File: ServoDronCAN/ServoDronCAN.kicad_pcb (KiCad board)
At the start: 2 copper layers, 80 x 87 mm, 13 parts, among them J2 Conn_01x02_Pin, J3 Conn_01x02_Pin, Q1 IRF9530N, U2 LM2575BU-ADJ

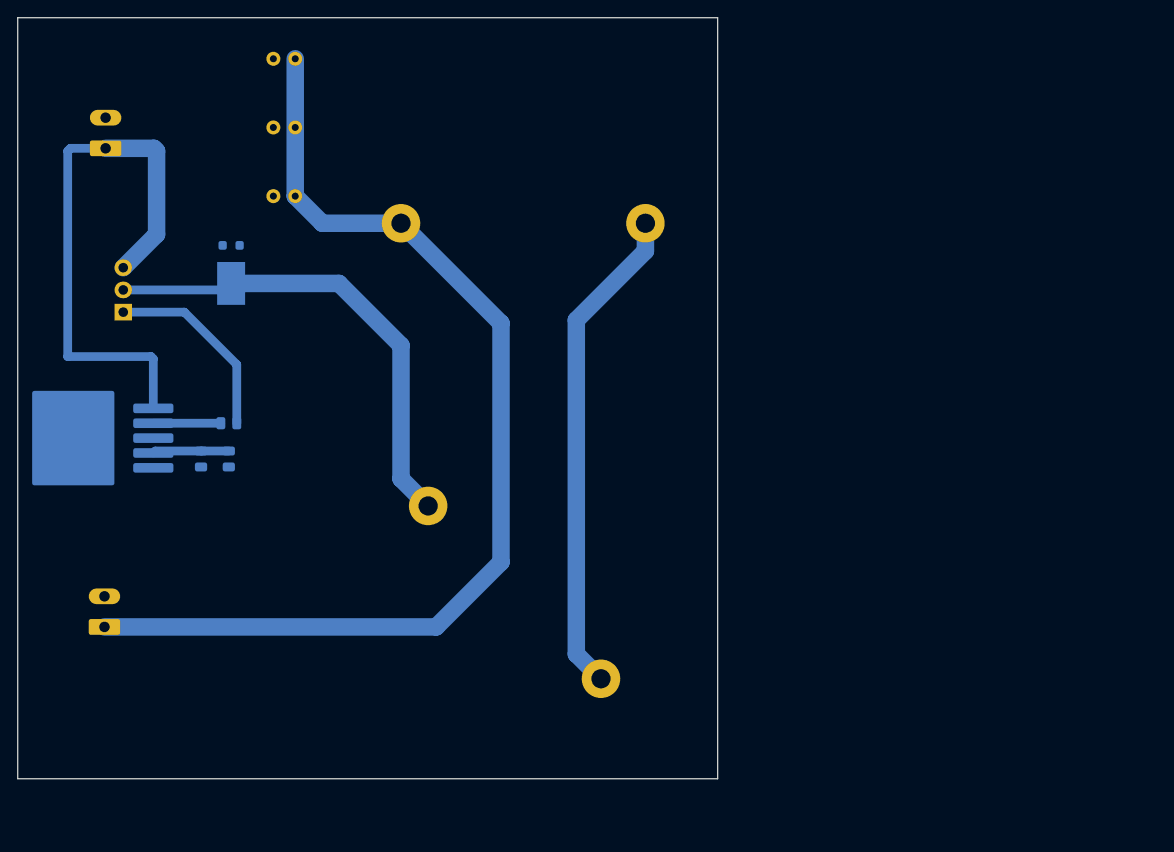
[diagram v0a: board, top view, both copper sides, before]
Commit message: Доработана электрическая схема (изменен частотный выход, добавлен разъем для питания вентилтора. Создана печатная плата с расположением компонентов.
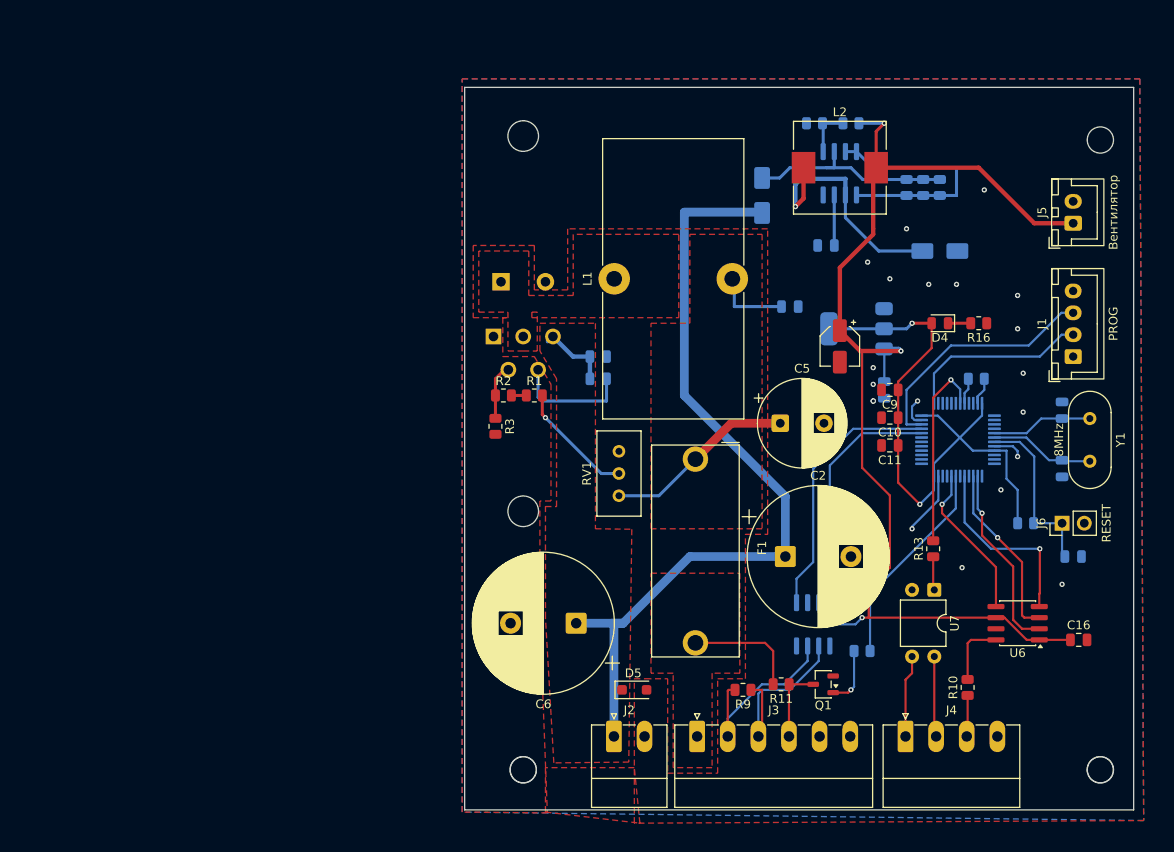
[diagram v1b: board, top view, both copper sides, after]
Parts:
- added ?: , , F.Cu at (227.9, 125.3)
- added ?: , , F.Cu at (161.9, 125.3)
- added ?: , , F.Cu at (227.9, 53.3)
- added C10: 1uF, Capacitor_SMD:C_0805_2012Metric, F.Cu at (203.8, 85.1)
- added C11: 10uF, Capacitor_SMD:C_0805_2012Metric, F.Cu at (203.8, 88.3)
- added C12: 16pF, Capacitor_SMD:C_0805_2012Metric, B.Cu at (223.5, 84.2)
- added C13: 16pF, Capacitor_SMD:C_0805_2012Metric, B.Cu at (223.5, 90.9)
- added C14: 100nF, Capacitor_SMD:C_0805_2012Metric, B.Cu at (203.2, 81.9)
- added C15: 0.1uF, Capacitor_SMD:C_0805_2012Metric, B.Cu at (224.8, 101.0)
- added C16: 1uF, Capacitor_SMD:C_0805_2012Metric, F.Cu at (225.4, 110.5)
- added C4: 1uF, Capacitor_SMD:C_0805_2012Metric, B.Cu at (192.4, 72.4)
- added C5: 1mF/25V, Capacitor_THT:CP_Radial_D10.0mm_P5.00mm, F.Cu at (191.3, 85.7)
- added C6: 470uF/100V, Capacitor_THT:CP_Radial_D16.0mm_P7.50mm, F.Cu at (168.0, 108.6)
- added C7: 470pF, Capacitor_SMD:C_0805_2012Metric, B.Cu at (196.5, 65.4)
- added C8: 10uF, Capacitor_SMD:CP_Elec_4x5.4, F.Cu at (198.1, 76.9)
- added C9: 100nF, Capacitor_SMD:C_0805_2012Metric, F.Cu at (203.8, 81.9)
- added D2: GS1B, Diode_SMD:D_SMA, B.Cu at (189.2, 59.7)
- added D3: SS14, Diode_SMD:D_SMA, B.Cu at (209.6, 66.0)
- added D4: LED, LED_SMD:LED_0805_2012Metric, F.Cu at (209.6, 74.3)
- added D5: BZT52B36, Diode_SMD:D_SOD-123F, F.Cu at (174.6, 116.2)
- added F1: FH-101C, MAS_Package_nostd:FH-101C, F.Cu at (181.6, 89.8)
- added J1: PROG, Connector_JST:JST_XH_B4B-XH-A_1x04_P2.50mm_Vertical, F.Cu at (224.8, 78.1)
- added J4: Измерение, Connector_Phoenix_MC:PhoenixContact_MC_1,5_4-G-3.5_1x04_P3.50mm_Horizontal, F.Cu at (205.6, 121.5)
- added J5: Вентилятор, Connector_JST:JST_XH_B2B-XH-A_1x02_P2.50mm_Vertical, F.Cu at (224.8, 62.9)
- added J6: RESET, Connector_PinHeader_2.54mm:PinHeader_1x02_P2.54mm_Vertical, F.Cu at (223.5, 97.2)
- added R10: 1k, Resistor_SMD:R_0805_2012Metric, F.Cu at (212.7, 115.9)
- added R11: 300, Resistor_SMD:R_0805_2012Metric, F.Cu at (191.4, 115.6)
- added R12: 660, Resistor_SMD:R_0805_2012Metric, B.Cu at (200.7, 111.8)
- added R13: 660, Resistor_SMD:R_0805_2012Metric, F.Cu at (208.8, 100.1)
- added R14: 10k, Resistor_SMD:R_0805_2012Metric, B.Cu at (219.4, 97.2)
- added R15: 10k, Resistor_SMD:R_0805_2012Metric, B.Cu at (213.7, 80.6)
- added R16: 1k, Resistor_SMD:R_0805_2012Metric, F.Cu at (214.0, 74.3)
- added R4: 1, Resistor_SMD:R_0805_2012Metric, B.Cu at (205.7, 58.8)
- added R5: 1, Resistor_SMD:R_0805_2012Metric, B.Cu at (209.6, 58.8)
- added R6: 1, Resistor_SMD:R_0805_2012Metric, B.Cu at (207.6, 58.8)
- added R7: 3.6k, Resistor_SMD:R_0805_2012Metric, B.Cu at (199.4, 51.4)
- added R8: 1.2k, Resistor_SMD:R_0805_2012Metric, B.Cu at (195.2, 51.4)
- added R9: 120, Resistor_SMD:R_0805_2012Metric, F.Cu at (187.0, 116.2)
- added RV1: 10k, Potentiometer_THT:Potentiometer_Bourns_3296W_Vertical, F.Cu at (172.9, 88.9)
- added U1: STM32F103C8T6, Package_QFP:LQFP-48_7x7mm_P0.5mm, B.Cu at (211.6, 87.6)
- added U3: MC33063AD, Package_SO:SOIC-8_3.9x4.9mm_P1.27mm, B.Cu at (198.1, 57.1)
- added U5: CA-IF1042LVS, Package_SO:SOIC-8_3.9x4.9mm_P1.27mm, B.Cu at (195.1, 108.7)
- added U6: MCP4921, Package_SO:SOIC-8_3.9x4.9mm_P1.27mm, F.Cu at (218.4, 108.6)
- added U7: PC817, Package_DIP:DIP-4_W7.62mm, F.Cu at (208.9, 104.8)
- added U8: AMS1117, Package_TO_SOT_SMD:SOT-223-3_TabPin2, B.Cu at (200.0, 74.9)
- added Y1: 8MHz, Crystal:Crystal_HC49-U_Vertical, F.Cu at (226.7, 85.2)
- C1, C3: value 47uF/25V -> 1uF; footprint Capacitor_THT:C_Radial_D6.3mm_H7.0mm_P2.50mm -> Capacitor_SMD:C_0805_2012Metric
- C2: value 47uF/25V -> 470uF/100V; footprint Capacitor_THT:C_Radial_D6.3mm_H7.0mm_P2.50mm -> Capacitor_THT:CP_Radial_D16.0mm_P7.50mm; moved to F.Cu
- D1: value 10S45SP -> MBR1545; footprint Package_TO_SOT_SMD:TO-277B -> Package_TO_SOT_THT:TO-220-2_Horizontal_TabUp
- J2: value Conn_01x02_Pin -> Вход питания; moved to F.Cu
- J3: value Conn_01x02_Pin -> Управление; footprint Connector_Phoenix_MC:PhoenixContact_MC_1,5_2-G-3.5_1x02_P3.50mm_Horizontal -> Connector_Phoenix_MC:PhoenixContact_MC_1,5_6-G-3.5_1x06_P3.50mm_Horizontal; moved to F.Cu
- L1: footprint Inductor_THT:L_Radial_D40.6mm_P27.94mm_Vishay_IHB-4 -> Inductor_THT:L_Toroid_Vertical_L31.8mm_W15.9mm_P13.50mm_Bourns_5700; moved to F.Cu
- L2: value 47uH -> 200uF; footprint Inductor_THT:L_Radial_D40.6mm_P27.94mm_Vishay_IHB-4 -> Inductor_SMD:L_10.4x10.4_H4.8; moved to F.Cu
- Q1: value IRF9530N -> 2N7002; footprint Package_TO_SOT_THT:TO-220-3_Vertical -> Package_TO_SOT_SMD:SOT-23-3; moved to F.Cu
- R1: value 40R -> 1.5k; moved to F.Cu
- R2: value ~0-20k -> 1.5k; moved to F.Cu
- R3: value 2k -> 1.5k; moved to F.Cu
- U2: value LM2575BU-ADJ -> XL4016E1; footprint Package_TO_SOT_SMD:TO-263-5_TabPin3 -> Package_TO_SOT_THT:TO-220-5_P3.4x3.8mm_StaggerOdd_Lead7.13mm_TabDown
- moved Q1 90.6 mm to (196.2, 115.6), turned to 180 degrees
- moved J2 88.9 mm to (172.3, 121.5), turned to 0 degrees
- moved C2 74.5 mm to (191.9, 101.0), turned to 0 degrees
- moved J3 68.9 mm to (181.8, 121.5), turned to 0 degrees
- moved C1 50.4 mm to (170.5, 80.6), turned to 0 degrees
- moved U2 48.0 mm to (158.5, 75.8), turned to 0 degrees
- moved C3 39.2 mm to (170.5, 78.1), turned to 0 degrees
- moved R2 35.3 mm to (159.7, 82.5), turned to 0 degrees
- moved R1 35.1 mm to (163.2, 82.5)
- moved L1 33.6 mm to (172.3, 69.2), turned to 90 degrees
- moved D1 30.9 mm to (159.4, 69.6), turned to 0 degrees
- moved R3 30.7 mm to (158.8, 86.1), turned to -90 degrees
- moved L2 23.1 mm to (198.1, 56.5), turned to 0 degrees
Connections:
- C1 pad 1: /+Vout -> /+Vin
- C1 pad 2: GNDD -> Net-(U2-VC)
- C2 pad 1: /+Vout -> /+Vin
- C3 pad 1: /+Vout -> /+Vin
- D1 pad 1: GNDD -> Net-(D1-K)
- J3 pad 1: /+Vout -> /V_servoOut
- J3 pad 2: GNDD -> /CanH
- L1 pad 2: Net-(L1-Pad2) -> Net-(C4-Pad1)
- L2 pad 1: Net-(L1-Pad2) -> Net-(D3-K)
- L2 pad 2: /+Vout -> /+5V
- Q1 pad 2: Net-(D1-K) -> GNDD
- Q1 pad 3: /+Vin -> /PWM_Out
- R1 pad 1: Net-(U2-OUT) -> Net-(R1-Pad1)
- R1 pad 2: Net-(Q1-G) -> Net-(R1-Pad2)
- R2 pad 2: /+Vout -> Net-(R1-Pad1)
- R3 pad 1: GNDD -> Net-(U2-FB)
- R3 pad 2: Net-(U2-FB) -> GNDD
- U2 pad 1: /+Vin -> GNDD
- U2 pad 2: Net-(U2-OUT) -> Net-(U2-FB)
- U2 pad 3: GNDD -> Net-(D1-K)
- U2 pad 4: Net-(U2-FB) -> Net-(U2-VC)
- U2 pad 5: GNDD -> /+Vin
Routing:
- net /+5V: track 0.00 -> 132.1 mm, vias 0 -> 3
- net /+Vout: track 120.9 -> 0.00 mm
- net /+3.3V: track 0.00 -> 70.0 mm, vias 0 -> 2
- net Net-(L1-Pad2): track 56.5 -> 0.00 mm
- net Net-(D1-K): track 54.6 -> 0.00 mm
- net /+Vin: track 64.4 -> 102.8 mm
- net Net-(C4-Pad1): track 0.00 -> 30.5 mm
- net /C_TXD: track 0.00 -> 30.4 mm
- net /SWDIO: track 0.00 -> 28.4 mm
- net Net-(D3-K): track 0.00 -> 28.2 mm, vias 0 -> 1
- net Net-(U3-DC): track 0.00 -> 28.1 mm
- net /C_RXD: track 0.00 -> 27.7 mm
- net Net-(D2-K): track 0.00 -> 24.1 mm
- net /TIM3_CH4: track 0.00 -> 24.0 mm
- net /TIM4_CH2: track 0.00 -> 22.3 mm, vias 0 -> 1
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- added copper zone on F.Cu, net /+Vin
- added copper zone on F.Cu, net /V_servoOut
- added copper zone on B.Cu, net GNDD
- added copper zone on F.Cu, net GNDD
- added copper zone on F.Cu, net Net-(C4-Pad1)
- added copper zone on F.Cu, net Net-(D1-K)
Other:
- board size 80 x 87 mm -> 76.5 x 82.6 mm
- board text added: "+Vпит"
- board text added: "+ПИТ"
- board text added: "0-10"
- board text added: "CH"
- board text added: "CL"
- board text added: "Col"
- board text added: "Em"
- board text added: "GND"
- board text added: "PWM"

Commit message: Исправлена электрическая схема. Добвлена защита от переполюсовки и предохранитель от превышение потребляемоготока (6А). Создан гербер файл для производства.
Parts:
- removed D5: BZT52B36, Diode_SMD:D_SOD-123F
- removed J5: Вентилятор, Connector_JST:JST_XH_B2B-XH-A_1x02_P2.50mm_Vertical
- added D6: VS-6CWQ10FNTR-M3, Package_TO_SOT_SMD:TO-252-2, B.Cu at (173.1, 101.2)
- moved F1 25.6 mm to (178.4, 115.3), turned to 90 degrees
- moved R8 10.8 mm to (205.7, 54.0), turned to 90 degrees
- moved L2 6.98 mm to (198.1, 63.5)
- moved R7 4.58 mm to (203.2, 54.0), turned to -90 degrees
- moved C6 4.52 mm to (163.8, 106.8), turned to -90 degrees
- turned RV1 to 180 degrees
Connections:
- C4 pad 1: Net-(C4-Pad1) -> /V_servoOut
- C5 pad 1: Net-(C4-Pad1) -> /V_servoOut
- F1 pad 1: Net-(C4-Pad1) -> Net-(J2-Pin_1)
- F1 pad 2: /V_servoOut -> /+Vin
- J2 pad 1: /+Vin -> Net-(J2-Pin_1)
- J3 pad 5: GNDD -> /+5V
- L1 pad 2: Net-(C4-Pad1) -> /V_servoOut
- RV1 pad 3: Net-(C4-Pad1) -> /V_servoOut
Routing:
- net /+Vin: track 102.8 -> 63.9 mm, vias 0 -> 35
- net Net-(C4-Pad1): track 30.5 -> 0.00 mm
- net /+5V: track 132.1 -> 120.0 mm
- net /V_servoOut: track 13.1 -> 23.5 mm
- net Net-(U3-Vfb): track 5.62 -> 14.1 mm
- net Net-(R1-Pad2): track 13.7 -> 17.4 mm
- net Net-(D3-K): track 28.2 -> 26.3 mm
- net Net-(U3-DC): track 28.1 -> 28.8 mm
- net GNDD: vias 21 -> 20
- added copper zone on B.Cu, net /+Vin
- added copper zone on F.Cu, net Net-(J2-Pin_1)
- removed copper zone on F.Cu, net Net-(C4-Pad1)
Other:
- board size 76.5 x 82.6 mm -> 75 x 80 mm
- board text added: "+5V"
